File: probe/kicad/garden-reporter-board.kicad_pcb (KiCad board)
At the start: 2 copper layers, 40.6 x 88.9 mm, 22 parts, among them J1 70543-0106, J2 Conn_01x02, J3 70543-0002, J4 70543-0002, J5 70543-0002, Q1 TN0702N3-G, U1 MCP1700-3302E_TO92, U2 MCP1700-3302E_TO92

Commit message: Feature/v divider for sensors
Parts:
- added R3: 10K 1%, Resistor_THT:R_Axial_DIN0207_L6.3mm_D2.5mm_P7.62mm_Horizontal, F.Cu at (160.9, 127.5)
- added R4: 5K 1%, Resistor_THT:R_Axial_DIN0207_L6.3mm_D2.5mm_P7.62mm_Horizontal, F.Cu at (160.8, 124.0)
- J5: footprint Connector_Molex:Molex_SL_171971-0003_1x03_P2.54mm_Vertical -> Connector_Molex:Molex_SL_171971-0002_1x02_P2.54mm_Vertical
- R2: value 10K 1% -> 2K 1%
- R5: renamed from R3; value 10K 1% -> 180 1%
- moved R5 22.5 mm to (165.9, 99.3), turned to 180 degrees
- moved J2 19.9 mm to (146.3, 88.1), turned to -90 degrees
- moved D2 10.7 mm to (159.5, 94.7)
- moved R2 9.32 mm to (159.4, 91.0)
- moved J5 8.50 mm to (162.9, 105.6)
- moved R1 7.82 mm to (159.2, 87.2)
- moved J4 6.81 mm to (159.7, 116.4)
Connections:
- J3 pad 2: /sensor_soil -> Net-(J3-Pad2)
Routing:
- net GND1: track 171.2 -> 219.0 mm
- net Net-(J2-Pad1): track 45.2 -> 22.6 mm
- net Net-(J2-Pad2): track 43.8 -> 25.1 mm
- net /sensor_batt: track 60.4 -> 42.9 mm
- net +3.3VADC: track 76.6 -> 92.8 mm
- net /sensor_light: track 55.1 -> 40.0 mm
- net +BATT: track 44.7 -> 52.2 mm
- net /sensor_temp: track 59.1 -> 52.3 mm
- net Net-(J3-Pad2): track 0.00 -> 6.06 mm
- net /sensor_soil: track 71.7 -> 74.4 mm
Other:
- board text added: "Batt lvl"
- board text added: "Garden Reporter Probe bastien auneau - Sep 2022"
- board text added: "Power"
- board text removed: "Batt level"
- board text removed: "Garden Reporter Probe bastien auneau - Aug 2022"

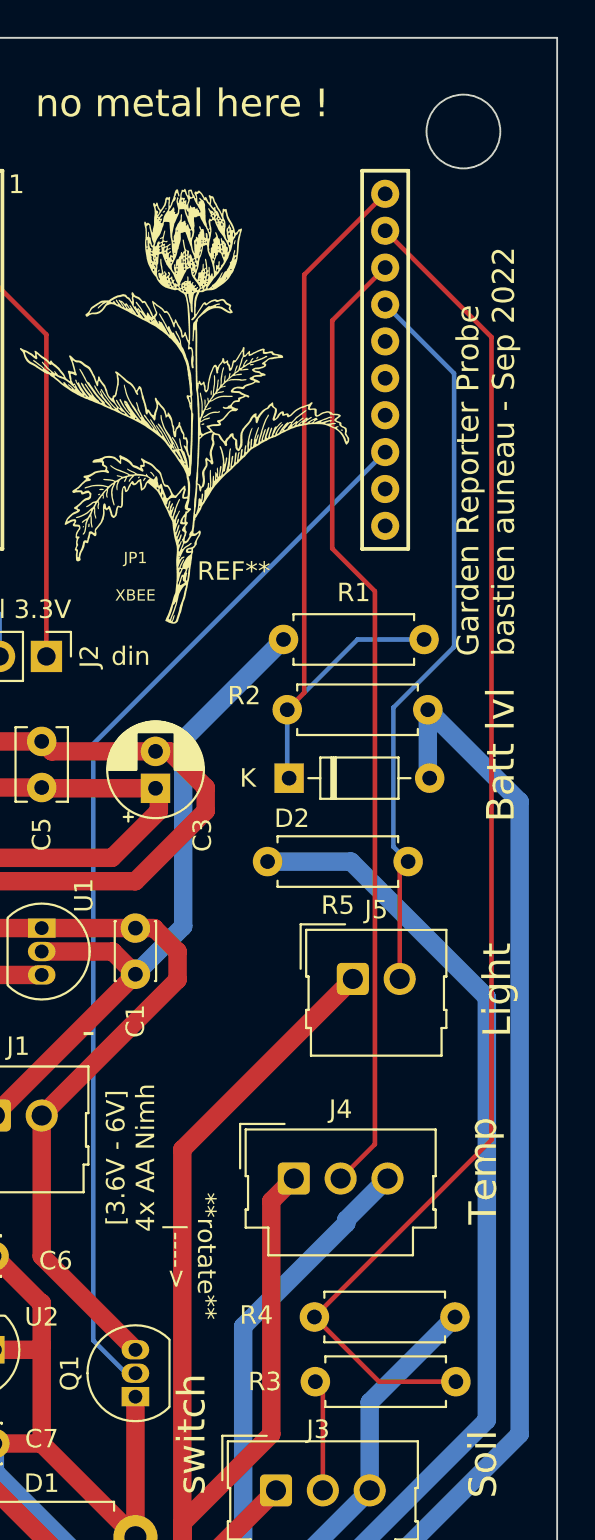
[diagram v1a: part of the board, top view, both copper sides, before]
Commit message: Add to light sensor V reg to 1.2V, adjust light R properly, fix layout accordingly
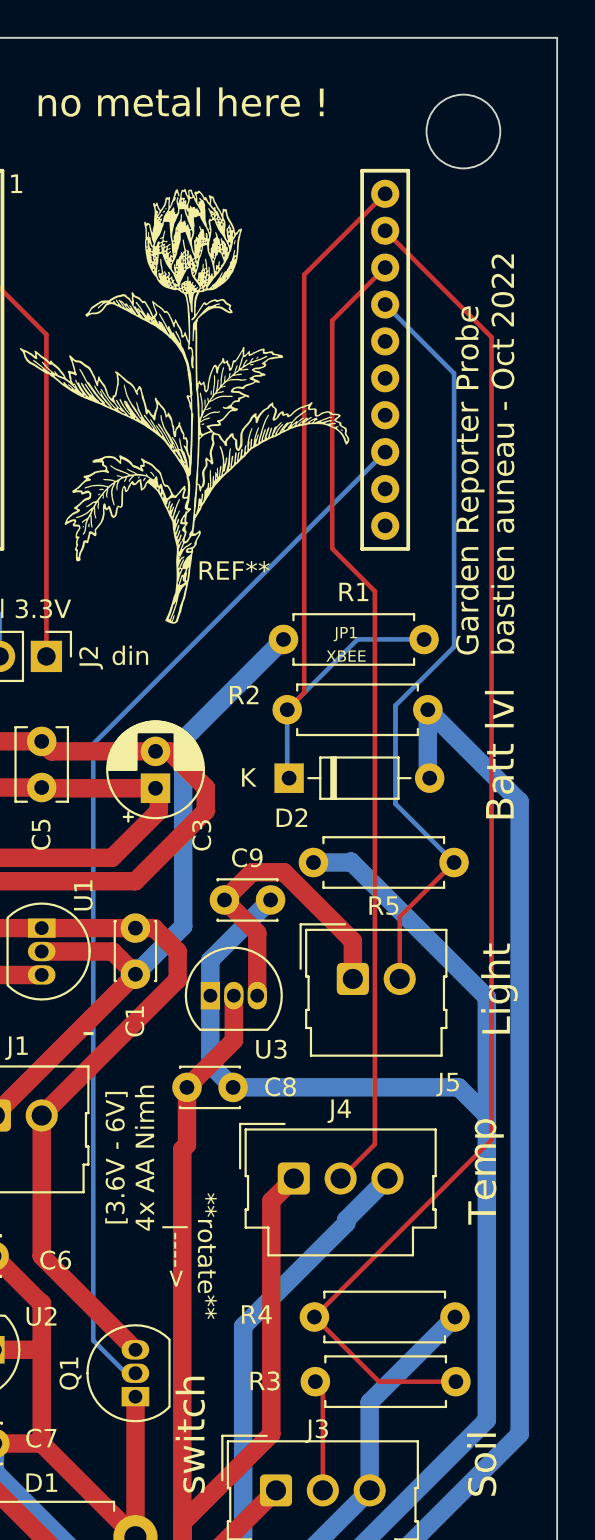
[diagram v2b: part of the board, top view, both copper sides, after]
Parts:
- added C8: 1uF, Capacitor_THT:C_Disc_D3.0mm_W2.0mm_P2.50mm, F.Cu at (153.9, 111.5)
- added C9: 1uF, Capacitor_THT:C_Disc_D3.0mm_W2.0mm_P2.50mm, F.Cu at (156.0, 101.3)
- added U3: MCP1700-1202E_TO92, Package_TO_SOT_THT:TO-92_Inline, F.Cu at (155.2, 106.5)
- R5: value 180 1% -> 68 1%
- moved R5 2.49 mm to (168.4, 99.3)
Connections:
- J5 pad 1: +3.3VADC -> +1V2
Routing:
- net GND1: track 219.0 -> 242.9 mm
- net +1V2: track 0.00 -> 17.1 mm
- net +3.3VADC: track 92.8 -> 89.2 mm
- net /sensor_light: track 40.0 -> 42.0 mm
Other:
- board text added: "Garden Reporter Probe bastien auneau - Oct 2022"
- board text removed: "Garden Reporter Probe bastien auneau - Sep 2022"

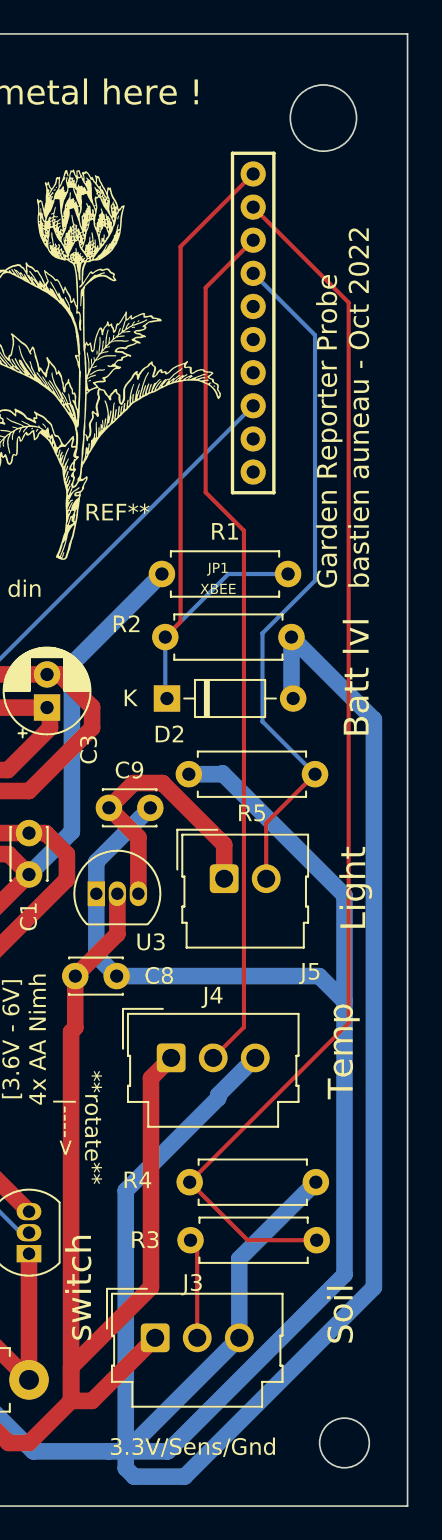
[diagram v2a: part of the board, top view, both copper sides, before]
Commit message: Fix voltage output range of soil moist sensor, 1.2V to light sensor
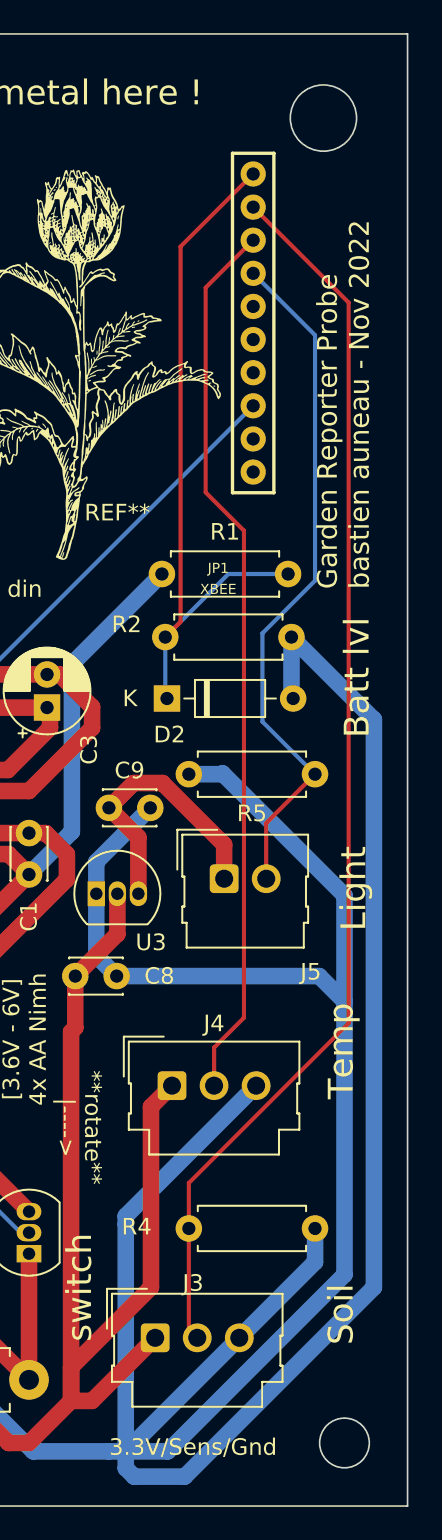
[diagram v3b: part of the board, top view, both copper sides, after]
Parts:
- removed R3: 10K 1%, Resistor_THT:R_Axial_DIN0207_L6.3mm_D2.5mm_P7.62mm_Horizontal
- R4: value 5K 1% -> 17K 1%
- moved R4 2.79 mm to (160.8, 126.7)
- moved J4 1.68 mm to (159.8, 118.1)
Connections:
- J3 pad 2: Net-(J3-Pad2) -> /sensor_soil
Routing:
- net Net-(J3-Pad2): track 6.06 -> 0.00 mm
- net GND1: track 242.9 -> 238.2 mm
- net +3.3VADC: track 89.2 -> 87.6 mm
- net /sensor_temp: track 52.3 -> 54.0 mm
- net /sensor_soil: track 74.4 -> 74.9 mm
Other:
- board text added: "Garden Reporter Probe bastien auneau - Nov 2022"
- board text removed: "Garden Reporter Probe bastien auneau - Oct 2022"

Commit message: More profile and dashbord backup
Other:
- board text added: "Ideas : * put xbee cap closer ? * check trace width for power"
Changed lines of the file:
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@@
     (effects (font (size 1.5 1.5) (thickness 0.3)))
+  )
+  (gr_text "Ideas : \n * put xbee cap closer ?\n * check trace width for power" (at 183.896 80.01) (layer "F.SilkS")
+    (effects (font (size 1.5 1.5) (thickness 0.3)) (justify left))
   )
   (gr_text "+" (at 140.716 108.204) (layer "F.SilkS")

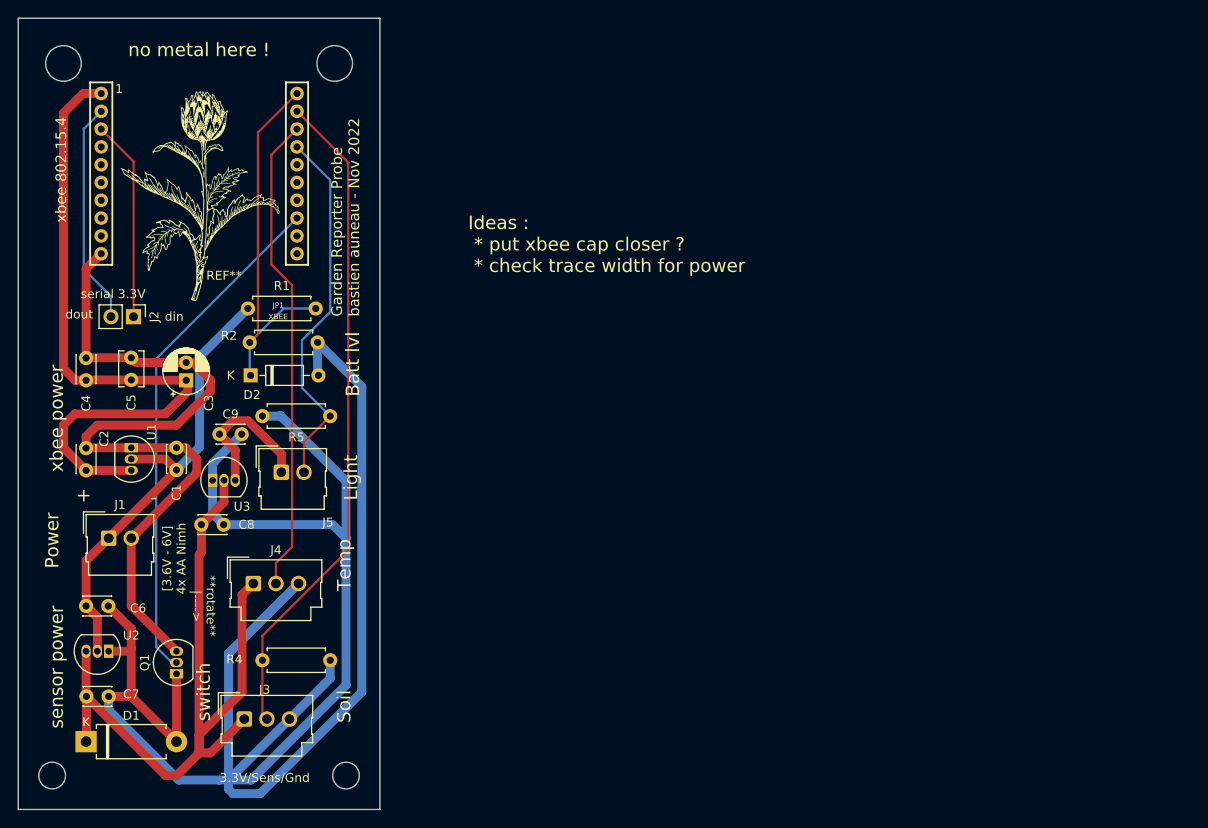
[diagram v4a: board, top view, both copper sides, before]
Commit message: Smaller profile. Re-number sensor mosfet pins properly
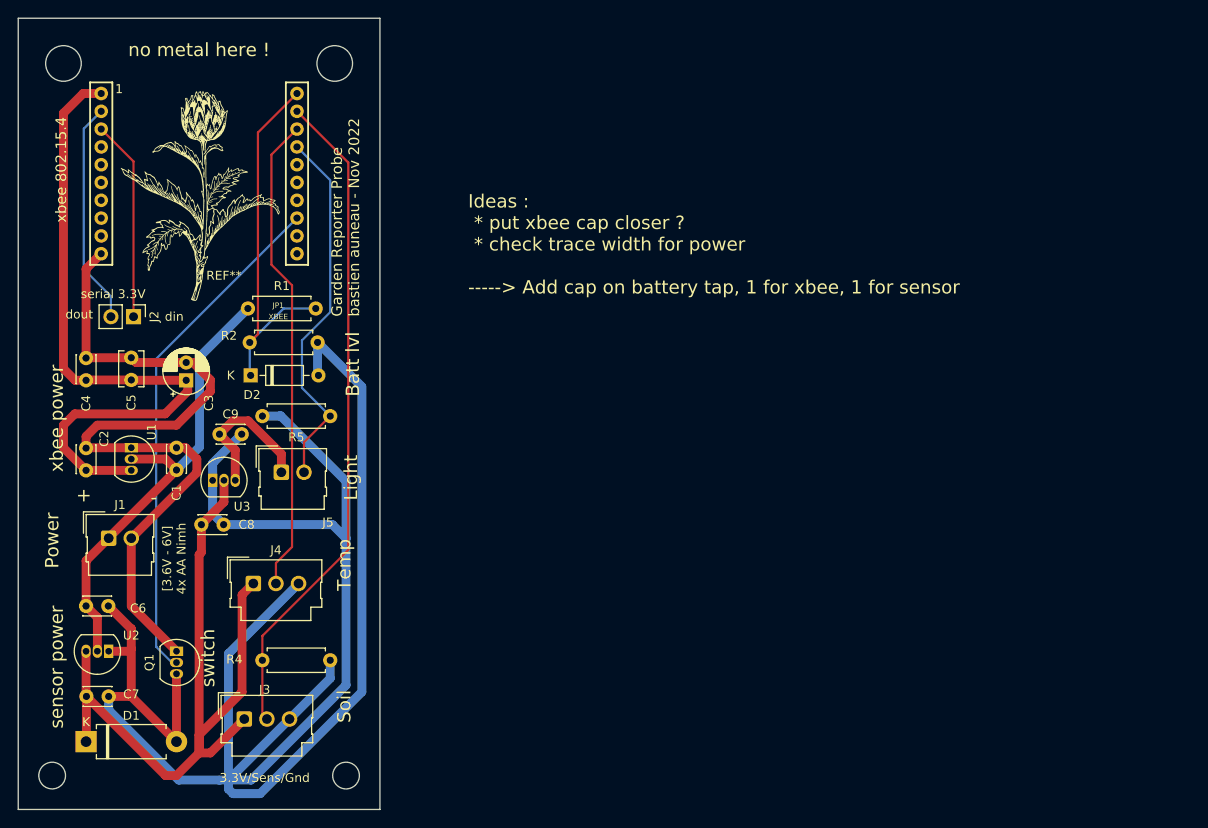
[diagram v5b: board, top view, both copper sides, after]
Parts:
- moved Q1 2.54 mm to (151.1, 125.7), turned to -90 degrees
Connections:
- Q1 pad 1: GND1 -> -BATT
- Q1 pad 3: -BATT -> GND1
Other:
- board text added: "Ideas : * put xbee cap closer ? * check trace width for power -----> Add cap on battery tap, 1 for xbee, 1 for sensor"
- board text removed: "**rotate** |---->"
- board text removed: "Ideas : * put xbee cap closer ? * check trace width for power"
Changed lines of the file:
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@@
       (effects (font (size 1.016 1.016) (thickness 0.1524)))
     )
-    (fp_line (start -12.24788 -0.7493) (end -9.74852 -0.7493) (layer "F.SilkS") (width 0.2032))
-    (fp_line (start 12.24788 -21.24964) (end 12.24788 -0.7493) (layer "F.SilkS") (width 0.2032))
     (fp_line (start -9.74852 -21.24964) (end -9.74852 -0.7493) (layer "F.SilkS") (width 0.2032))
-    (fp_line (start 12.24788 -0.7493) (end 9.74852 -0.7493) (layer "F.SilkS") (width 0.2032))
+    (fp_line (start 12.24788 -21.24964) (end 12.24788 -0.7493) (layer "F.SilkS") (width 0.2032))
+    (fp_line (start -9.74852 -21.24964) (end -12.24788 -21.24964) (layer "F.SilkS") (width 0.2032))
+    (fp_line (start -12.24788 -0.7493) (end -9.74852 -0.7493) (layer "F.SilkS") (width 0.2032))
     (fp_line (start 9.74852 -21.24964) (end 12.24788 -21.24964) (layer "F.SilkS") (width 0.2032))
-    (fp_line (start 9.74852 -21.24964) (end 9.74852 -0.7493) (layer "F.SilkS") (width 0.2032))
     (fp_line (start -12.24788 -21.24964) (end -12.24788 -0.7493) (layer "F.SilkS") (width 0.2032))
-    (fp_line (start -9.74852 -21.24964) (end -12.24788 -21.24964) (layer "F.SilkS") (width 0.2032))
-    (fp_line (start -12.24788 6.2484) (end 12.24788 6.2484) (layer "Dwgs.User") (width 0.127))
+    (fp_line (start 12.24788 -0.7493) (end 9.74852 -0.7493) (layer "F.SilkS") (width 0.2032))
+    (fp_line (start 9.74852 -21.24964) (end 9.74852 -0.7493) (layer "F.SilkS") (width 0.2032))
     (fp_line (start 12.24788 -21.24964) (end 4.99872 -27.59964) (layer "Dwgs.User") (width 0.127))
-    (fp_line (start -12.24788 -0.7493) (end -12.24788 0) (layer "Dwgs.User") (width 0.127))
     (fp_line (start -12.24788 0) (end -12.24788 6.2484) (layer "Dwgs.User") (width 0.127))
-    (fp_line (start -12.24788 0) (end 12.24788 0) (layer "Dwgs.User") (width 0.127))
+    (fp_line (start -4.99872 -27.59964) (end 4.99872 -27.59964) (layer "Dwgs.User") (width 0.127))
+    (fp_line (start -12.24788 6.2484) (end 12.24788 6.2484) (layer "Dwgs.User") (width 0.127))
     (fp_line (start 12.24788 0) (end 12.24788 6.2484) (layer "Dwgs.User") (width 0.127))
+    (fp_line (start -12.24788 -0.7493) (end -12.24788 0) (layer "Dwgs.User") (width 0.127))
     (fp_line (start -12.24788 -21.24964) (end -4.99872 -27.59964) (layer "Dwgs.User") (width 0.127))
+    (fp_line (start -12.24788 0) (end 12.24788 0) (layer "Dwgs.User") (width 0.127))
     (fp_line (start 12.24788 -0.7493) (end 12.24788 0) (layer "Dwgs.User") (width 0.127))
-    (fp_line (start -4.99872 -27.59964) (end 4.99872 -27.59964) (layer "Dwgs.User") (width 0.127))
     (pad "1" thru_hole circle locked (at -10.9982 -19.99996) (size 1.524 1.524) (drill 0.79756) (layers *.Cu *.Mask)
       (net 3 "+3.3V") (pinfunction "VDD") (pintype "power_in") (solder_mask_margin 0.1016))
@@
   )
   (footprint "Package_TO_SOT_THT:TO-92_Inline" (layer "F.Cu")
-    (at 151.13 128.27 90)
+    (at 151.13 125.73 -90)
     (descr "TO-92 leads in-line, narrow, oval pads, drill 0.75mm (see NXP sot054_po.pdf)")
     (tags "to-92 sc-43 sc-43a sot54 PA33 transistor")
     (property "Sheetfile" "garden-reporter-board.kicad_sch")
     (property "Sheetname" "")
+    (property "Spice_Model" "TN0702N3-G")
+    (property "Spice_Netlist_Enabled" "Y")
+    (property "Spice_Primitive" "M")
     (attr through_hole)
-    (fp_text reference "Q1" (at 1.27 -3.56 90) (layer "F.SilkS")
+    (fp_text reference "Q1" (at 1.27 3.048 90) (layer "F.SilkS")
       (effects (font (size 1 1) (thickness 0.15)))
     )
@@
     (fp_arc (start 1.27 -2.48) (mid 3.561221 -0.949055) (end 3.023625 1.753625) (layer "F.Fab") (width 0.1))
     (fp_arc (start -0.483625 1.753625) (mid -1.021221 -0.949055) (end 1.27 -2.48) (layer "F.Fab") (width 0.1))
-    (pad "1" thru_hole rect (at 0 0 90) (size 1.05 1.5) (drill 0.75) (layers *.Cu *.Mask)
-      (net 4 "GND1") (pinfunction "D") (pintype "passive"))
-    (pad "2" thru_hole oval (at 1.27 0 90) (size 1.05 1.5) (drill 0.75) (layers *.Cu *.Mask)
-      (net 20 "/xbee_ON") (pinfunction "G") (pintype "input"))
-    (pad "3" thru_hole oval (at 2.54 0 90) (size 1.05 1.5) (drill 0.75) (layers *.Cu *.Mask)
+    (pad "1" thru_hole rect (at 0 0 270) (size 1.05 1.5) (drill 0.75) (layers *.Cu *.Mask)
       (net 2 "-BATT") (pinfunction "S") (pintype "passive"))
+    (pad "2" thru_hole oval (at 1.27 0 270) (size 1.05 1.5) (drill 0.75) (layers *.Cu *.Mask)
+      (net 20 "/xbee_ON") (pinfunction "G") (pintype "input"))
+    (pad "3" thru_hole oval (at 2.54 0 270) (size 1.05 1.5) (drill 0.75) (layers *.Cu *.Mask)
+      (net 4 "GND1") (pinfunction "D") (pintype "passive"))
     (model "${KICAD6_3DMODEL_DIR}/Package_TO_SOT_THT.3dshapes/TO-92_Inline.wrl"
       (offset (xyz 0 0 0))
@@
     (effects (font (size 1.5 1.5) (thickness 0.3)))
   )
-  (gr_text "**rotate**\n|---->" (at 154.178 120.65 270) (layer "F.SilkS")
-    (effects (font (size 1 1) (thickness 0.15)))
-  )
   (gr_text "Light" (at 170.7388 106.2228 90) (layer "F.SilkS")
     (effects (font (size 1.5 1.5) (thickness 0.3)))
@@
     (effects (font (size 1.2 1.2) (thickness 0.15)))
   )
-  (gr_text "switch" (at 154.178 130.302 90) (layer "F.SilkS")
+  (gr_text "switch" (at 154.686 126.492 90) (layer "F.SilkS")
     (effects (font (size 1.5 1.5) (thickness 0.3)))
   )
-  (gr_text "Ideas : \n * put xbee cap closer ?\n * check trace width for power" (at 183.896 80.01) (layer "F.SilkS")
+  (gr_text "Ideas : \n * put xbee cap closer ?\n * check trace width for power\n\n-----> Add cap on battery tap, 1 for xbee, 1 for sensor" (at 183.896 80.01) (layer "F.SilkS")
     (effects (font (size 1.5 1.5) (thickness 0.3)) (justify left))
   )
